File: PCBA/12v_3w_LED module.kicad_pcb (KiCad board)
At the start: 2 copper layers, 73.7 x 22.9 mm, 9 parts, among them P1 Generic Pad, P2 Generic Pad, P3 Generic Pad, U1 NCR321ZX

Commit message: creadas las reglas de diseñor & DRC correcto
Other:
- rule pad_to_mask_clearance: 0 -> 0.05
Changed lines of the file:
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@@
   )
   (setup
-    (pad_to_mask_clearance 0)
+    (stackup
+      (layer "F.SilkS" (type "Top Silk Screen"))
+      (layer "F.Paste" (type "Top Solder Paste"))
+      (layer "F.Mask" (type "Top Solder Mask") (thickness 0.01))
+      (layer "F.Cu" (type "copper") (thickness 0.035))
+      (layer "dielectric 1" (type "core") (thickness 1.51) (material "FR4") (epsilon_r 4.5) (loss_tangent 0.02))
+      (layer "B.Cu" (type "copper") (thickness 0.035))
+      (layer "B.Mask" (type "Bottom Solder Mask") (thickness 0.01))
+      (layer "B.Paste" (type "Bottom Solder Paste"))
+      (layer "B.SilkS" (type "Bottom Silk Screen"))
+      (copper_finish "None")
+      (dielectric_constraints no)
+    )
+    (pad_to_mask_clearance 0.05)
+    (solder_mask_min_width 0.254)
     (pcbplotparams
       (layerselection 0x00010fc_ffffffff)

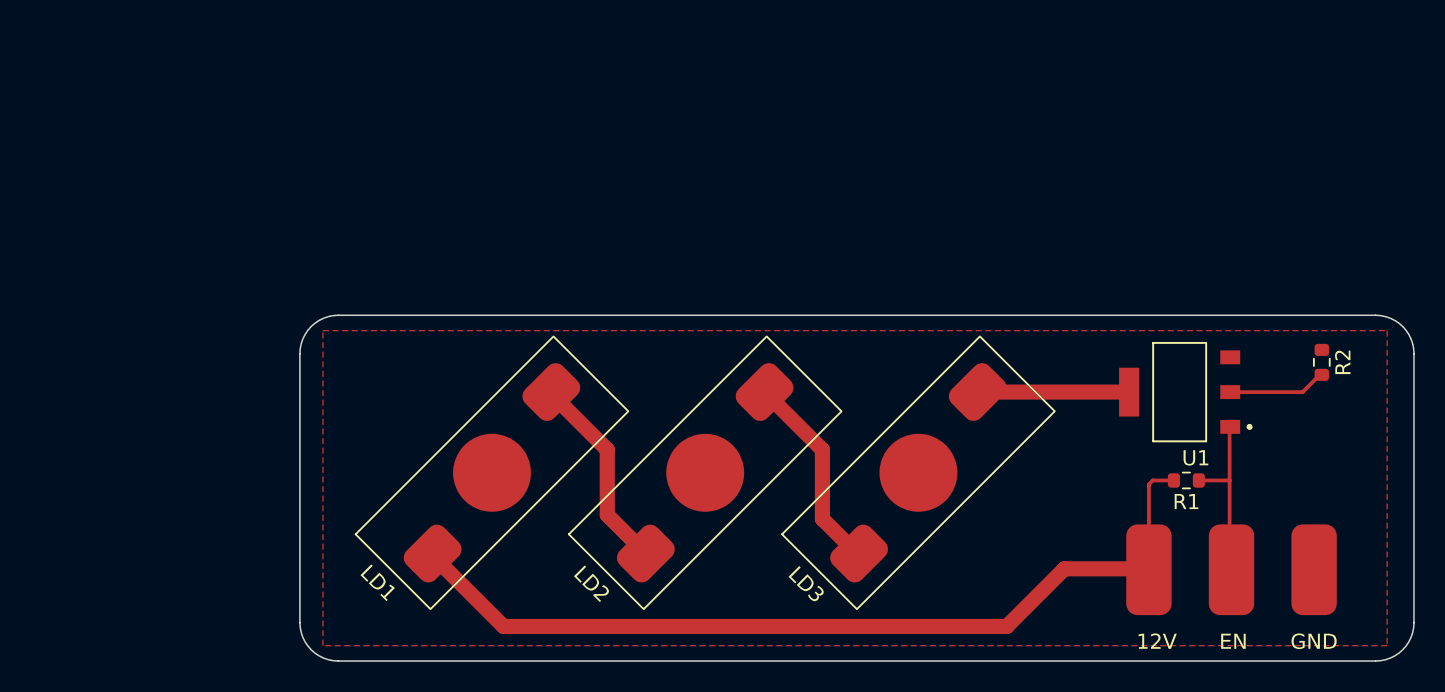
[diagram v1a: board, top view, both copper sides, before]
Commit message: añadido logo, fillet las esquinas y arreglado la polaridad de los LED
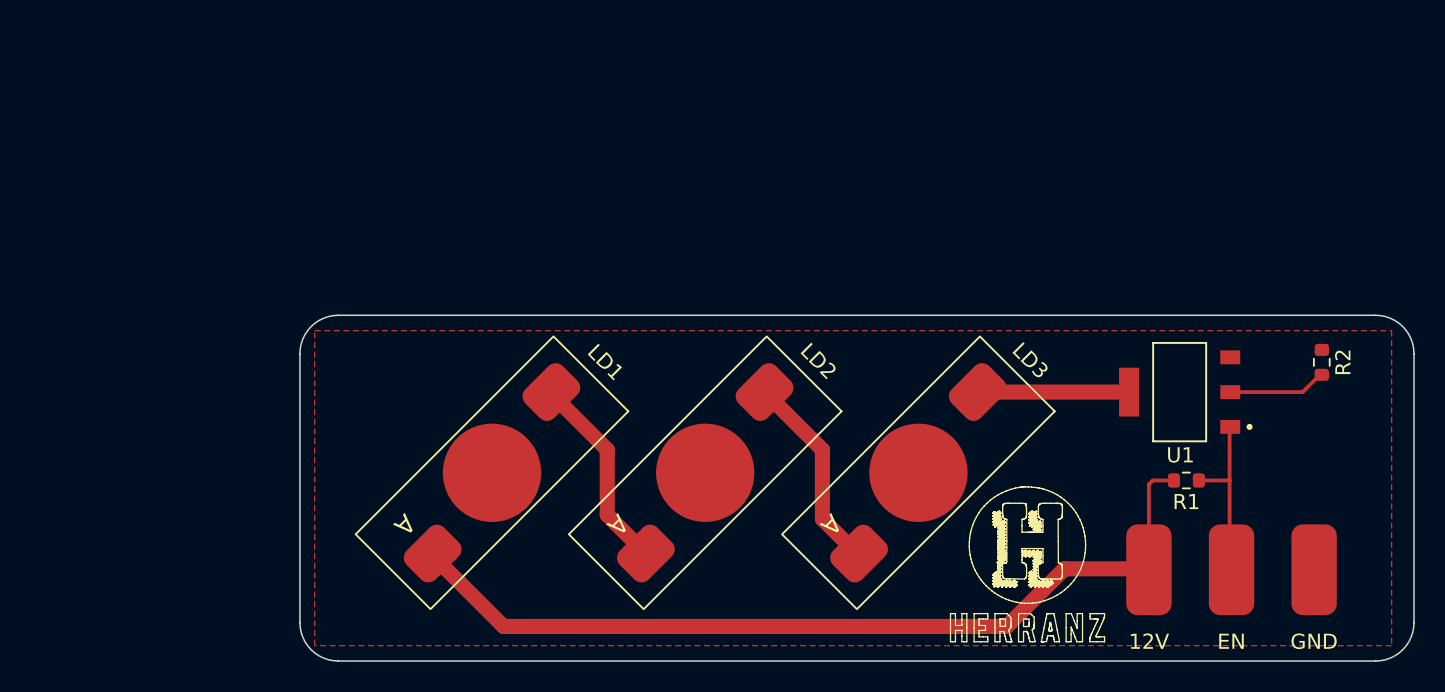
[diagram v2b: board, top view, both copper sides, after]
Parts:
- turned LD1 to -135 degrees
- turned LD2 to -135 degrees
- turned LD3 to -135 degrees

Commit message: finalizado el diseño
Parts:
- moved LD1 25.9 mm to (119.4, 111.0)
- moved LD2 25.9 mm to (133.5, 111.0)
- moved LD3 25.9 mm to (147.6, 111.0)
- moved R2 25.9 mm to (174.2, 103.7)
- moved P1 25.9 mm to (162.8, 117.4)
- moved P2 25.9 mm to (168.3, 117.4)
- moved P3 25.9 mm to (173.7, 117.4)
- moved R1 25.9 mm to (165.3, 111.5)
- moved U1 25.9 mm to (164.8, 105.7)
